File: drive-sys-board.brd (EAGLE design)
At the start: 109.9 x 49.5 mm, 23 parts, among them J1 APP_2POS_CONFIG12V_VERT, U1 OKI-78SR-5/1.5-W36HC

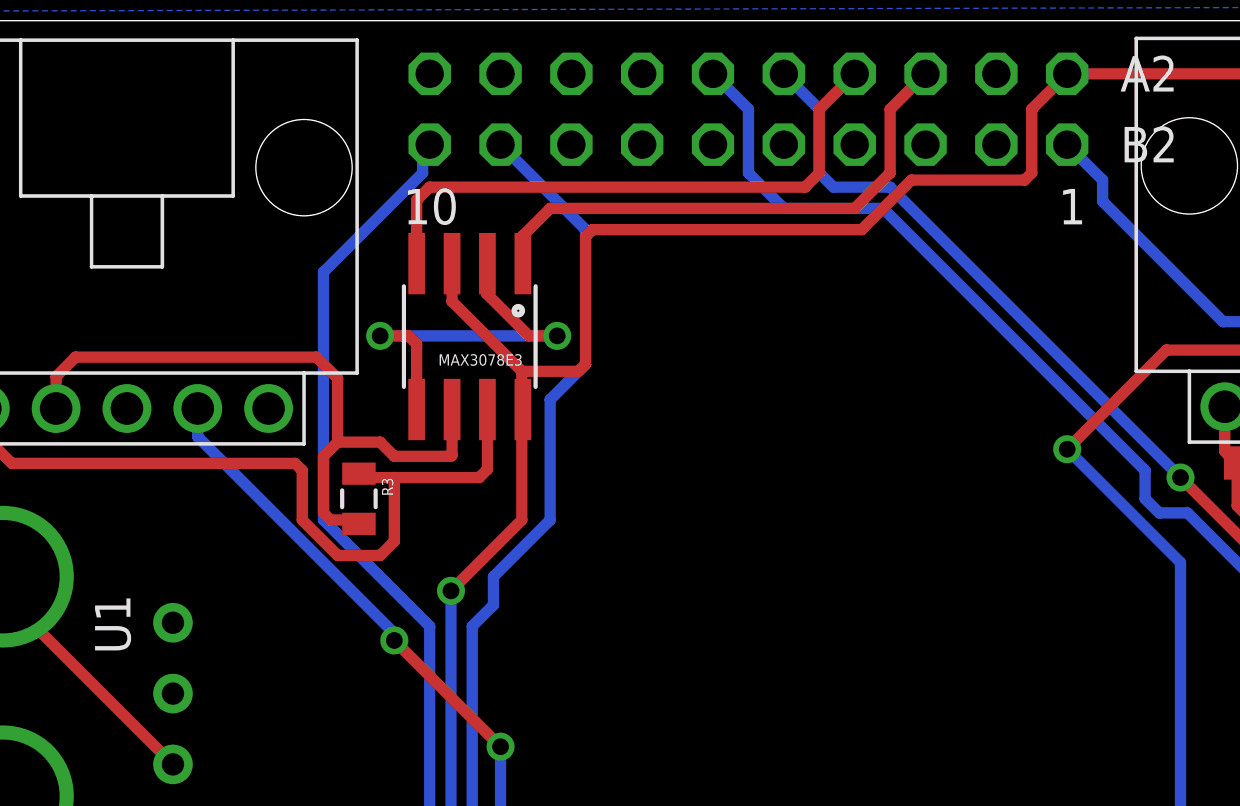
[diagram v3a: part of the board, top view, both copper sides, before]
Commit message: Changed named wire for 3V3 to supply symbol
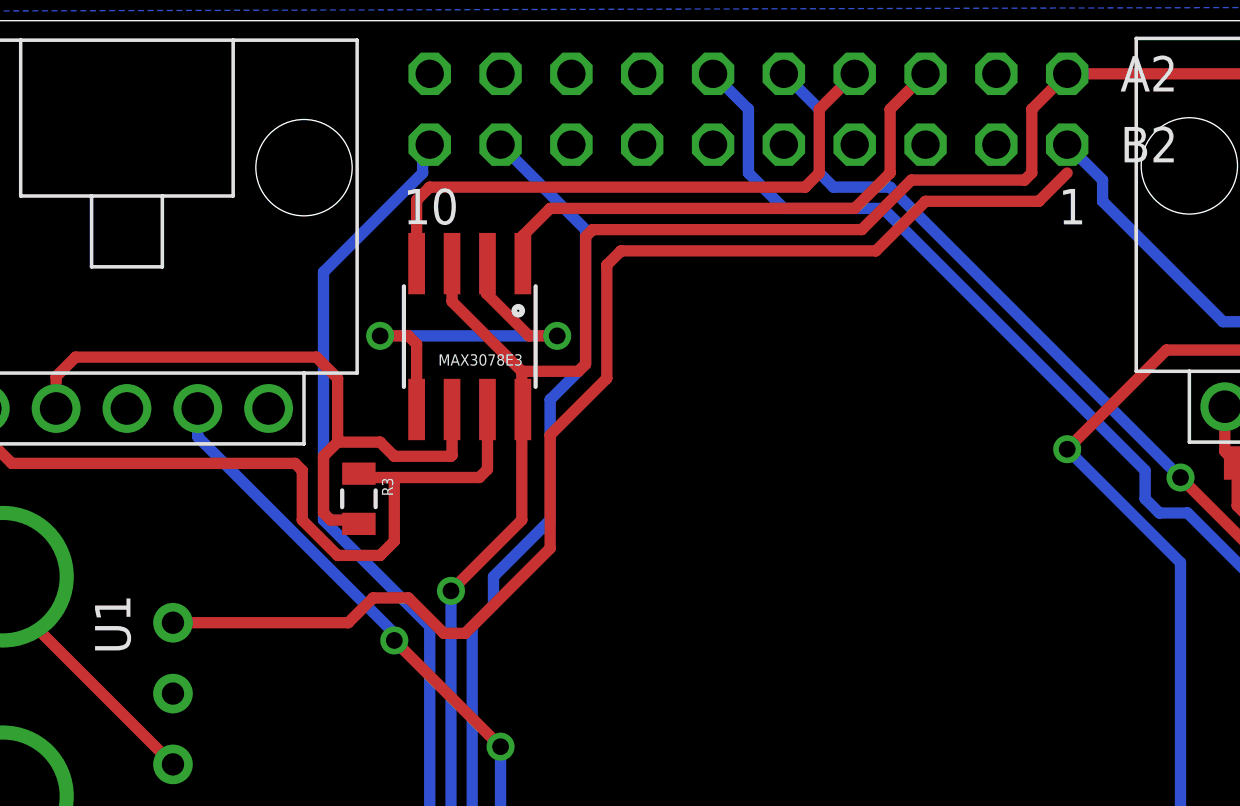
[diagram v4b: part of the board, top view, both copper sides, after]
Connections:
- removed net VCC: U$1.+5V_1, U$1.+5V_2
- net +5V: now also U$1.+5V_1, U$1.+5V_2
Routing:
- net +5V: track 0.00 -> 121.4 mm, vias 0 -> 2
- net VCC: track 76.9 -> 0.00 mm, vias 2 -> 0
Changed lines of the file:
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@@
 </polygon>
 <contactref element="U1" pad="3"/>
+<contactref element="U$1" pad="+5V_1"/>
+<contactref element="U$1" pad="+5V_2"/>
+<wire x1="44.45" y1="44.45" x2="45.72" y2="43.18" width="0.4064" layer="16"/>
+<wire x1="45.72" y1="43.18" x2="45.72" y2="42.418" width="0.4064" layer="16"/>
+<wire x1="45.72" y1="42.418" x2="50.038" y2="38.1" width="0.4064" layer="16"/>
+<wire x1="50.038" y1="38.1" x2="71.374" y2="38.1" width="0.4064" layer="16"/>
+<wire x1="71.374" y1="38.1" x2="74.168" y2="40.894" width="0.4064" layer="16"/>
+<wire x1="74.168" y1="40.894" x2="90.932" y2="40.894" width="0.4064" layer="16"/>
+<via x="90.932" y="40.894" extent="1-16" drill="0.6"/>
+<wire x1="90.932" y1="40.894" x2="93.218" y2="40.894" width="0.4064" layer="1"/>
+<via x="93.218" y="40.894" extent="1-16" drill="0.6"/>
+<wire x1="93.218" y1="40.894" x2="98.552" y2="40.894" width="0.4064" layer="16"/>
+<wire x1="98.552" y1="40.894" x2="103.124" y2="36.322" width="0.4064" layer="16"/>
+<wire x1="103.124" y1="36.322" x2="106.426" y2="36.322" width="0.4064" layer="16"/>
+<wire x1="106.426" y1="36.322" x2="107.95" y2="37.846" width="0.4064" layer="16"/>
+<wire x1="107.95" y1="37.846" x2="107.95" y2="44.45" width="0.4064" layer="16"/>
+<wire x1="12.3825" y1="27.305" x2="18.669" y2="27.305" width="0.4064" layer="1"/>
+<wire x1="18.669" y1="27.305" x2="19.558" y2="28.194" width="0.4064" layer="1"/>
+<wire x1="19.558" y1="28.194" x2="20.828" y2="28.194" width="0.4064" layer="1"/>
+<wire x1="20.828" y1="28.194" x2="22.098" y2="26.924" width="0.4064" layer="1"/>
+<wire x1="22.098" y1="26.924" x2="22.86" y2="26.924" width="0.4064" layer="1"/>
+<wire x1="22.86" y1="26.924" x2="25.908" y2="29.972" width="0.4064" layer="1"/>
+<wire x1="25.908" y1="29.972" x2="25.908" y2="34.036" width="0.4064" layer="1"/>
+<wire x1="25.908" y1="34.036" x2="27.94" y2="36.068" width="0.4064" layer="1"/>
+<wire x1="27.94" y1="36.068" x2="27.94" y2="40.132" width="0.4064" layer="1"/>
+<wire x1="27.94" y1="40.132" x2="28.448" y2="40.64" width="0.4064" layer="1"/>
+<wire x1="28.448" y1="40.64" x2="37.592" y2="40.64" width="0.4064" layer="1"/>
+<wire x1="37.592" y1="40.64" x2="39.37" y2="42.418" width="0.4064" layer="1"/>
+<wire x1="39.37" y1="42.418" x2="43.434" y2="42.418" width="0.4064" layer="1"/>
+<wire x1="43.434" y1="42.418" x2="44.45" y2="43.434" width="0.4064" layer="1"/>
 </signal>
 <signal name="PWM_6">
@@
 <wire x1="6.2865" y1="28.321" x2="12.3825" y2="22.225" width="0.4064" layer="1"/>
 </signal>
-<signal name="VCC">
-<contactref element="U$1" pad="+5V_1"/>
-<contactref element="U$1" pad="+5V_2"/>
-<wire x1="44.45" y1="44.45" x2="45.72" y2="43.18" width="0.4064" layer="16"/>
-<wire x1="45.72" y1="43.18" x2="45.72" y2="42.418" width="0.4064" layer="16"/>
-<wire x1="45.72" y1="42.418" x2="50.038" y2="38.1" width="0.4064" layer="16"/>
-<wire x1="50.038" y1="38.1" x2="71.374" y2="38.1" width="0.4064" layer="16"/>
-<wire x1="71.374" y1="38.1" x2="74.168" y2="40.894" width="0.4064" layer="16"/>
-<wire x1="74.168" y1="40.894" x2="90.932" y2="40.894" width="0.4064" layer="16"/>
-<via x="90.932" y="40.894" extent="1-16" drill="0.6"/>
-<wire x1="90.932" y1="40.894" x2="93.218" y2="40.894" width="0.4064" layer="1"/>
-<via x="93.218" y="40.894" extent="1-16" drill="0.6"/>
-<wire x1="93.218" y1="40.894" x2="98.552" y2="40.894" width="0.4064" layer="16"/>
-<wire x1="98.552" y1="40.894" x2="103.124" y2="36.322" width="0.4064" layer="16"/>
-<wire x1="103.124" y1="36.322" x2="106.426" y2="36.322" width="0.4064" layer="16"/>
-<wire x1="106.426" y1="36.322" x2="107.95" y2="37.846" width="0.4064" layer="16"/>
-<wire x1="107.95" y1="37.846" x2="107.95" y2="44.45" width="0.4064" layer="16"/>
-</signal>
 <signal name="+3V3">

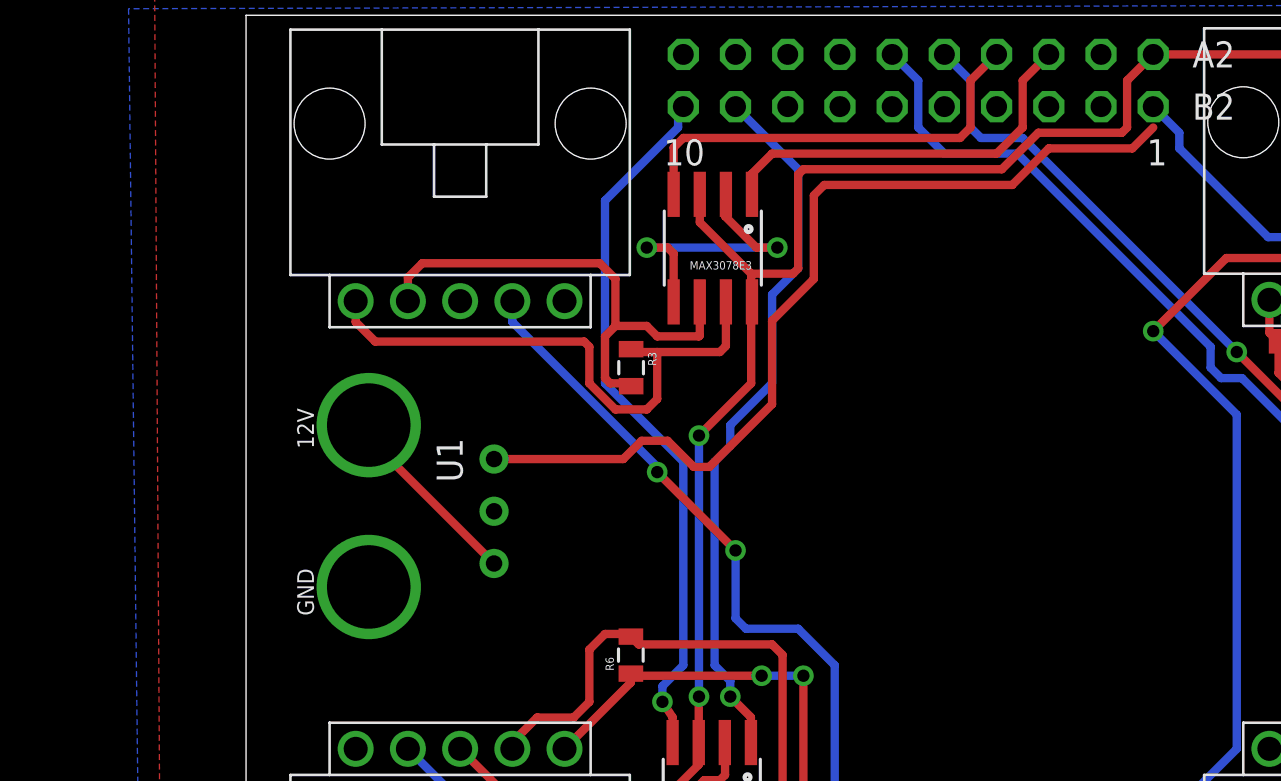
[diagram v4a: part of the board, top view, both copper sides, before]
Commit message: Switched vertical power connector for horizontal.
APP45_12V_VERT_CONFIG switched to APP45_12V_HORIZ_CONFIG
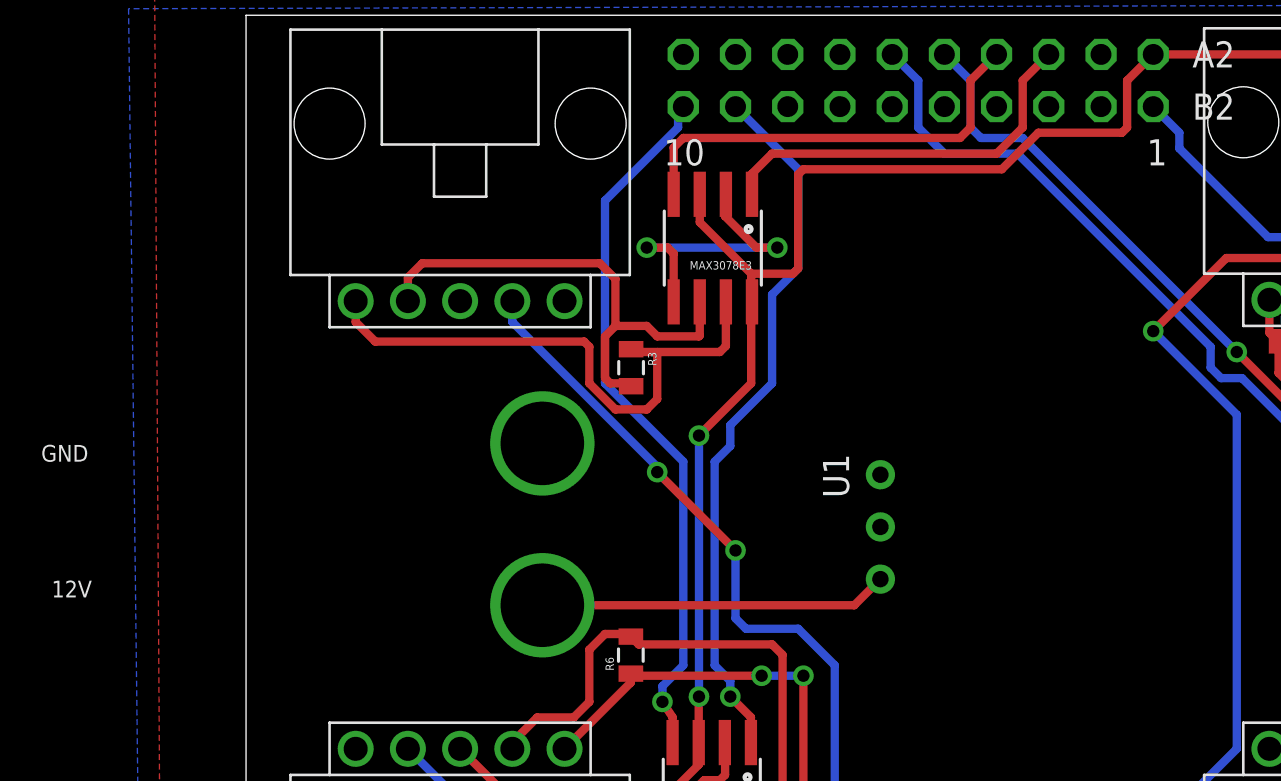
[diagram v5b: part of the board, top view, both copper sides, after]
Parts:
- removed J1: APP_2POS_CONFIG12V_VERT, MRDT-Connectors:APP45_12V_VERT_CONFIG
- added J2: APP_2POS_CONFIG12V_HORIZ, MRDT-Connectors:APP45_12V_HORIZ_CONFIG
- moved U1 18.8 mm to (31.2, 21.5)
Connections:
- net GND: now also J2.GND; no longer J1.GND
- net N$5: now also J2.12V; no longer J1.VCC
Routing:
- net +5V: track 121.4 -> 76.9 mm
- net N$5: track 9.26 -> 17.0 mm
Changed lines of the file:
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@@
 <element name="MAX3078E6" library="MRDT-ICs" package="SOIC8" value="MAX3078E" x="25.3365" y="12.7" rot="R180"/>
 <element name="R6" library="SparkFun-Passives" package="0805" value="120" x="19.0373" y="17.7673" rot="R90"/>
-<element name="U1" library="MRDT-ICs" package="OKI-78SR_HORIZ" value="OKI-78SR-5/1.5-W36HC" x="12.3825" y="22.225" rot="R270">
-<attribute name="VOUT" value="+5v" x="12.3825" y="22.225" size="1.778" layer="27" rot="R270" display="off"/>
+<element name="U1" library="MRDT-ICs" package="OKI-78SR_HORIZ" value="OKI-78SR-5/1.5-W36HC" x="31.1785" y="21.463" rot="R270">
+<attribute name="VOUT" value="+5v" x="31.1785" y="21.463" size="1.778" layer="27" rot="R270" display="off"/>
 </element>
-<element name="J1" library="MRDT-Connectors" package="APP45_12V_VERT_CONFIG" value="APP_2POS_CONFIG12V_VERT" x="1.5875" y="17.145">
-<attribute name="COLOR1" value="YELLOW" x="1.5875" y="17.145" size="1.778" layer="27" display="off"/>
-<attribute name="COLOR2" value="BLACK" x="1.5875" y="17.145" size="1.778" layer="27" display="off"/>
+<element name="J2" library="MRDT-Connectors" package="APP45_12V_HORIZ_CONFIG" value="APP_2POS_CONFIG12V_HORIZ" x="-13.462" y="16.256">
+<attribute name="COLOR1" value="YELLOW" x="-13.462" y="16.256" size="1.778" layer="27" display="off"/>
+<attribute name="COLOR2" value="BLACK" x="-13.462" y="16.256" size="1.778" layer="27" display="off"/>
 </element>
 </elements>
@@
 <contactref element="MAX3078E4" pad="5"/>
 <contactref element="U1" pad="2"/>
-<contactref element="J1" pad="GND"/>
 <contactref element="MAX3078E_1" pad="2"/>
 <contactref element="MAX3078E3" pad="2"/>
@@
 <wire x1="23.622" y1="40.1449" x2="23.6603" y2="40.1832" width="0.4064" layer="1"/>
 <wire x1="93.218" y1="7.874" x2="97.028" y2="7.874" width="0.4064" layer="1"/>
+<contactref element="J2" pad="GND"/>
 </signal>
 <signal name="TX_1">
@@
 <wire x1="106.426" y1="36.322" x2="107.95" y2="37.846" width="0.4064" layer="16"/>
 <wire x1="107.95" y1="37.846" x2="107.95" y2="44.45" width="0.4064" layer="16"/>
-<wire x1="12.3825" y1="27.305" x2="18.669" y2="27.305" width="0.4064" layer="1"/>
-<wire x1="18.669" y1="27.305" x2="19.558" y2="28.194" width="0.4064" layer="1"/>
-<wire x1="19.558" y1="28.194" x2="20.828" y2="28.194" width="0.4064" layer="1"/>
-<wire x1="20.828" y1="28.194" x2="22.098" y2="26.924" width="0.4064" layer="1"/>
-<wire x1="22.098" y1="26.924" x2="22.86" y2="26.924" width="0.4064" layer="1"/>
-<wire x1="22.86" y1="26.924" x2="25.908" y2="29.972" width="0.4064" layer="1"/>
-<wire x1="25.908" y1="29.972" x2="25.908" y2="34.036" width="0.4064" layer="1"/>
-<wire x1="25.908" y1="34.036" x2="27.94" y2="36.068" width="0.4064" layer="1"/>
-<wire x1="27.94" y1="36.068" x2="27.94" y2="40.132" width="0.4064" layer="1"/>
-<wire x1="27.94" y1="40.132" x2="28.448" y2="40.64" width="0.4064" layer="1"/>
-<wire x1="28.448" y1="40.64" x2="37.592" y2="40.64" width="0.4064" layer="1"/>
-<wire x1="37.592" y1="40.64" x2="39.37" y2="42.418" width="0.4064" layer="1"/>
-<wire x1="39.37" y1="42.418" x2="43.434" y2="42.418" width="0.4064" layer="1"/>
-<wire x1="43.434" y1="42.418" x2="44.45" y2="43.434" width="0.4064" layer="1"/>
 </signal>
 <signal name="PWM_6">
@@
 <signal name="N$5">
 <contactref element="U1" pad="1"/>
-<contactref element="J1" pad="VCC"/>
-<wire x1="6.2865" y1="28.956" x2="6.2865" y2="28.321" width="0.4064" layer="1"/>
-<wire x1="6.2865" y1="28.321" x2="12.3825" y2="22.225" width="0.4064" layer="1"/>
+<contactref element="J2" pad="12V"/>
+<wire x1="14.732" y1="20.193" x2="29.9085" y2="20.193" width="0.4064" layer="1"/>
+<wire x1="29.9085" y1="20.193" x2="31.1785" y2="21.463" width="0.4064" layer="1"/>
 </signal>
 <signal name="+3V3">
